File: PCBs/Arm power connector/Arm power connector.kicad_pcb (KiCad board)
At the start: 2 copper layers, 100 x 100 mm, 8 parts, among them J1 Conn_01x08, J2 Conn_01x02

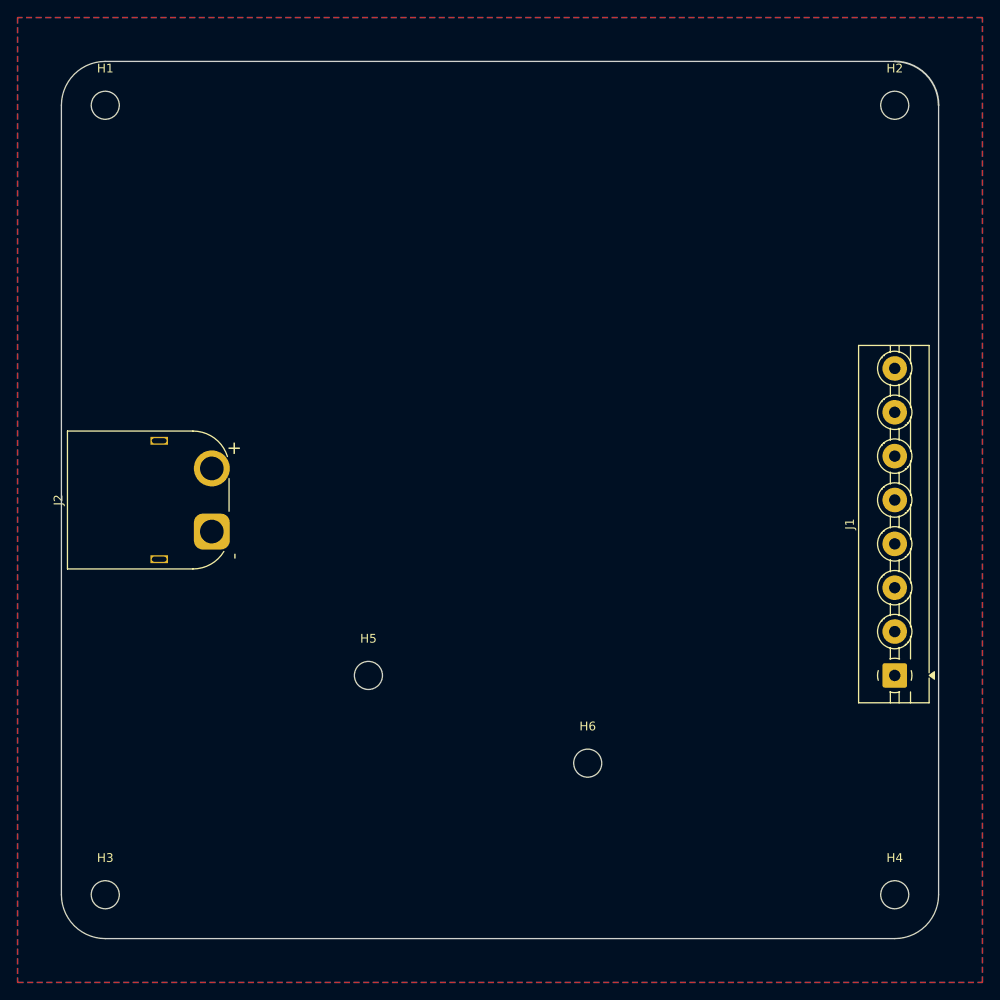
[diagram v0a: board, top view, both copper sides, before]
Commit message: DRC clean arm connector layout
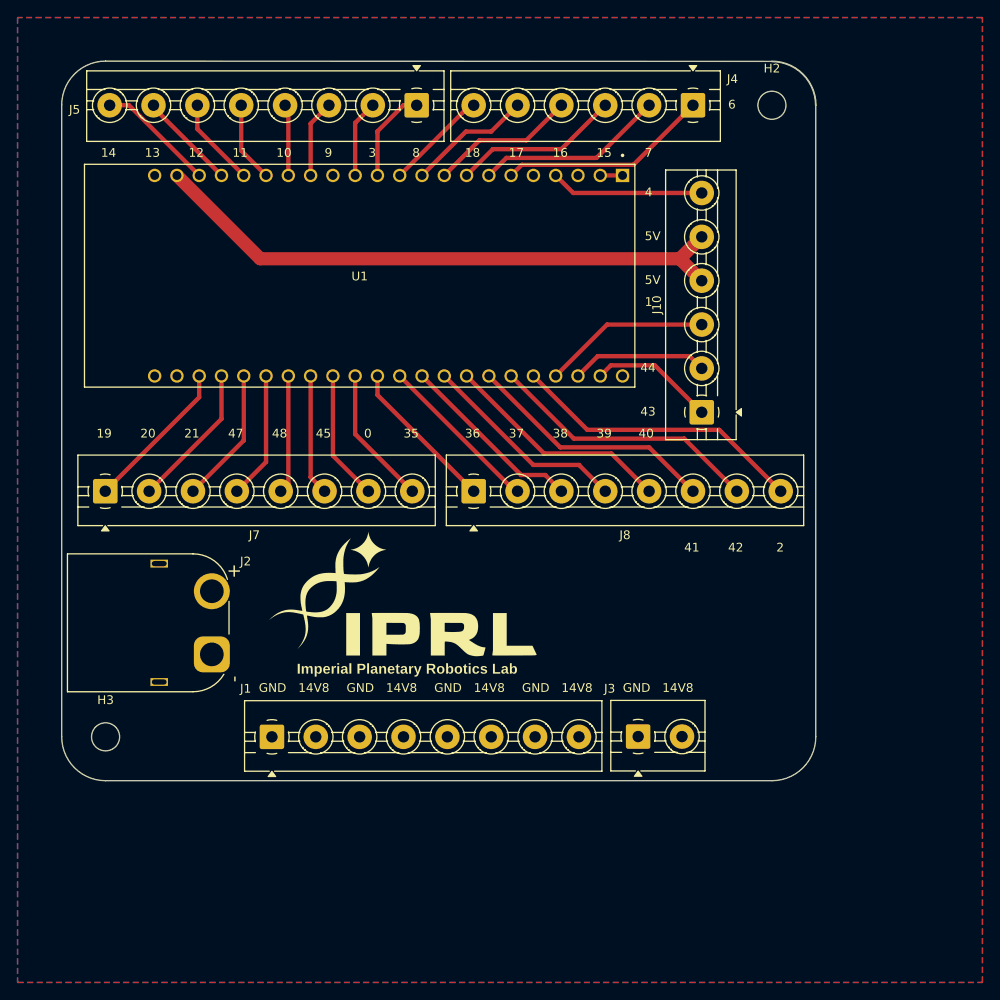
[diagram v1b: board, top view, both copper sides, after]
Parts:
- removed H1, H4, H5, H6: MountingHole, MountingHole:MountingHole_3.2mm_M3
- added G***: LOGO, main_lib:IPRL_31mm, F.Cu at (89.0, 112.0)
- added J10: Conn_01x06, TerminalBlock:TerminalBlock_MaiXu_MX126-5.0-06P_1x06_P5.00mm, F.Cu at (123.0, 90.0)
- added J3: Conn_01x02, TerminalBlock:TerminalBlock_MaiXu_MX126-5.0-02P_1x02_P5.00mm, F.Cu at (115.8, 127.0)
- added J4: Conn_01x06, TerminalBlock:TerminalBlock_MaiXu_MX126-5.0-06P_1x06_P5.00mm, F.Cu at (122.0, 55.0)
- added J5: Conn_01x08, TerminalBlock:TerminalBlock_MaiXu_MX126-5.0-08P_1x08_P5.00mm, F.Cu at (90.5, 55.0)
- added J7: Conn_01x08, TerminalBlock:TerminalBlock_MaiXu_MX126-5.0-08P_1x08_P5.00mm, F.Cu at (55.0, 99.0)
- added J8: Conn_01x08, TerminalBlock:TerminalBlock_MaiXu_MX126-5.0-08P_1x08_P5.00mm, F.Cu at (97.0, 99.0)
- added U1: ESP32-S3-DEVKITC-1U-N8R2, IPRL_Footprints:XCVR_ESP32-S3-DEVKITC-1U-N8R2, F.Cu at (84.0, 74.4)
- moved J1 71.3 mm to (74.0, 127.0), turned to 0 degrees
- moved H3 18.0 mm to (55.0, 127.0)
- moved H2 14.0 mm to (131.0, 55.0)
- moved J2 14.0 mm to (67.2, 117.6)
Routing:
- net /5V: track 0.00 -> 68.3 mm
- net /GPIO2: track 0.00 -> 33.6 mm
- net /GPIO42: track 0.00 -> 31.2 mm
- net /GPIO41: track 0.00 -> 28.7 mm
- net /GPIO40: track 0.00 -> 26.3 mm
- net /GPIO6: track 0.00 -> 24.0 mm
- net /GPIO39: track 0.00 -> 23.8 mm
- net /GPIO7: track 0.00 -> 21.6 mm
- net /GPIO38: track 0.00 -> 21.3 mm
- net /GPIO15: track 0.00 -> 19.1 mm
- net /GPIO1: track 0.00 -> 19.1 mm
- net /GPIO37: track 0.00 -> 18.9 mm
- net /GPIO36: track 0.00 -> 17.7 mm
- net /GPIO19: track 0.00 -> 17.6 mm
- net /GPIO4: track 0.00 -> 17.5 mm
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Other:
- board size 100 x 100 mm -> 86 x 82 mm
- board text added: "0"
- board text added: "1"
- board text added: "10"
- board text added: "11"
- board text added: "12"
- board text added: "13"
- board text added: "14"
- board text added: "14V8"
- board text added: "15"
- board text added: "16"
- board text added: "17"
- board text added: "18"
- board text added: "19"
- board text added: "2"
- board text added: "20"
- board text added: "21"
- board text added: "3"
- board text added: "35"
- board text added: "36"
- board text added: "37"
- board text added: "38"
- board text added: "39"
- board text added: "4"
- board text added: "40"
- board text added: "41"
- board text added: "42"
- board text added: "43"
- board text added: "44"
- board text added: "45"
- board text added: "47"
- board text added: "48"
- board text added: "5V"
- board text added: "6"
- board text added: "7"
- board text added: "8"
- board text added: "9"
- board text added: "Backup Arm Board"
- board text added: "Designed by James King"
- board text added: "GND"
